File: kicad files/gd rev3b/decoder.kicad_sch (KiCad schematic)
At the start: 18 parts, among them U25 SN74LVC573ANS

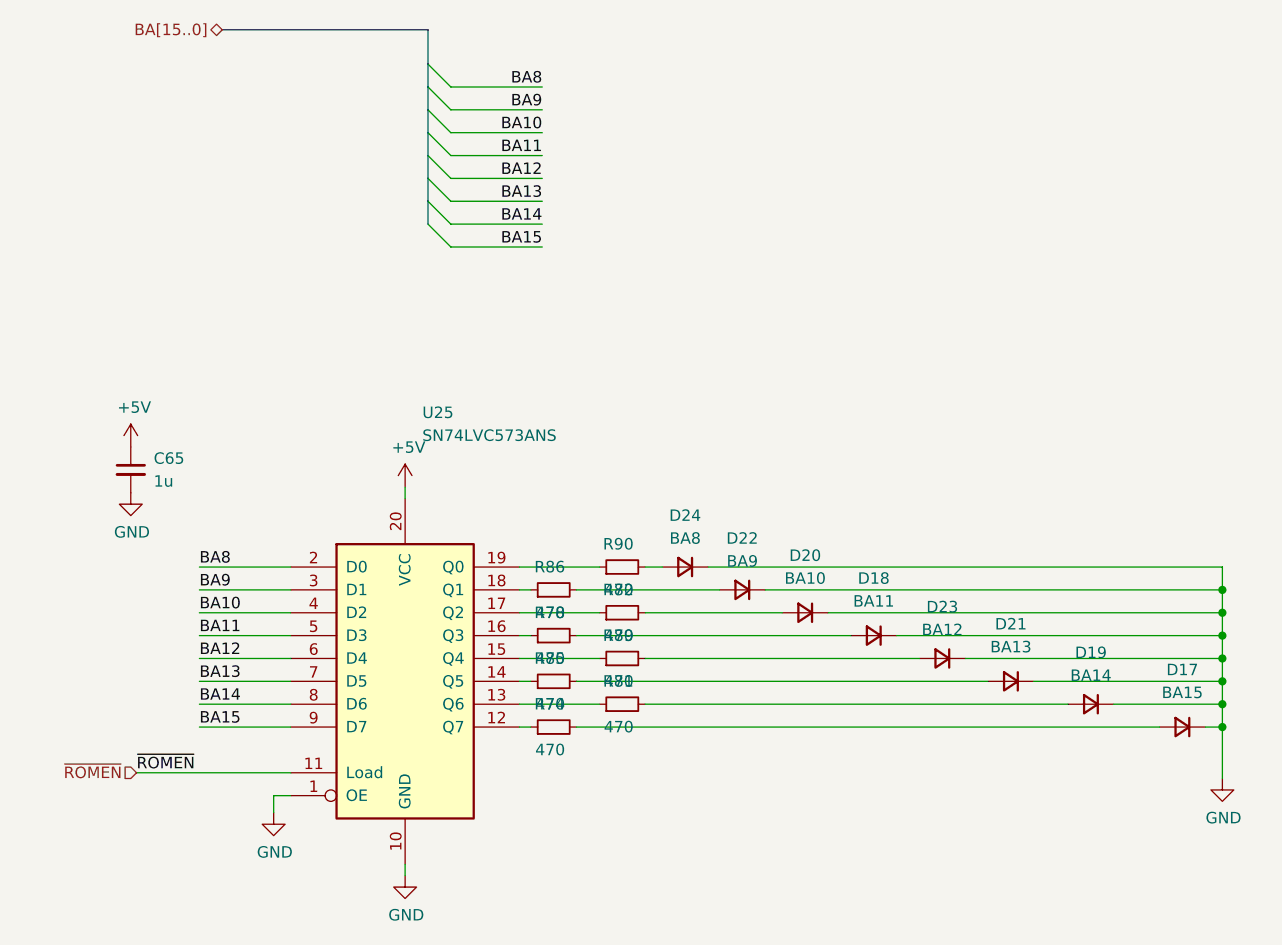
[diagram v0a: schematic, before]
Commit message: Schematic changes for #52, #50, #70, #51, #61, #69, #71
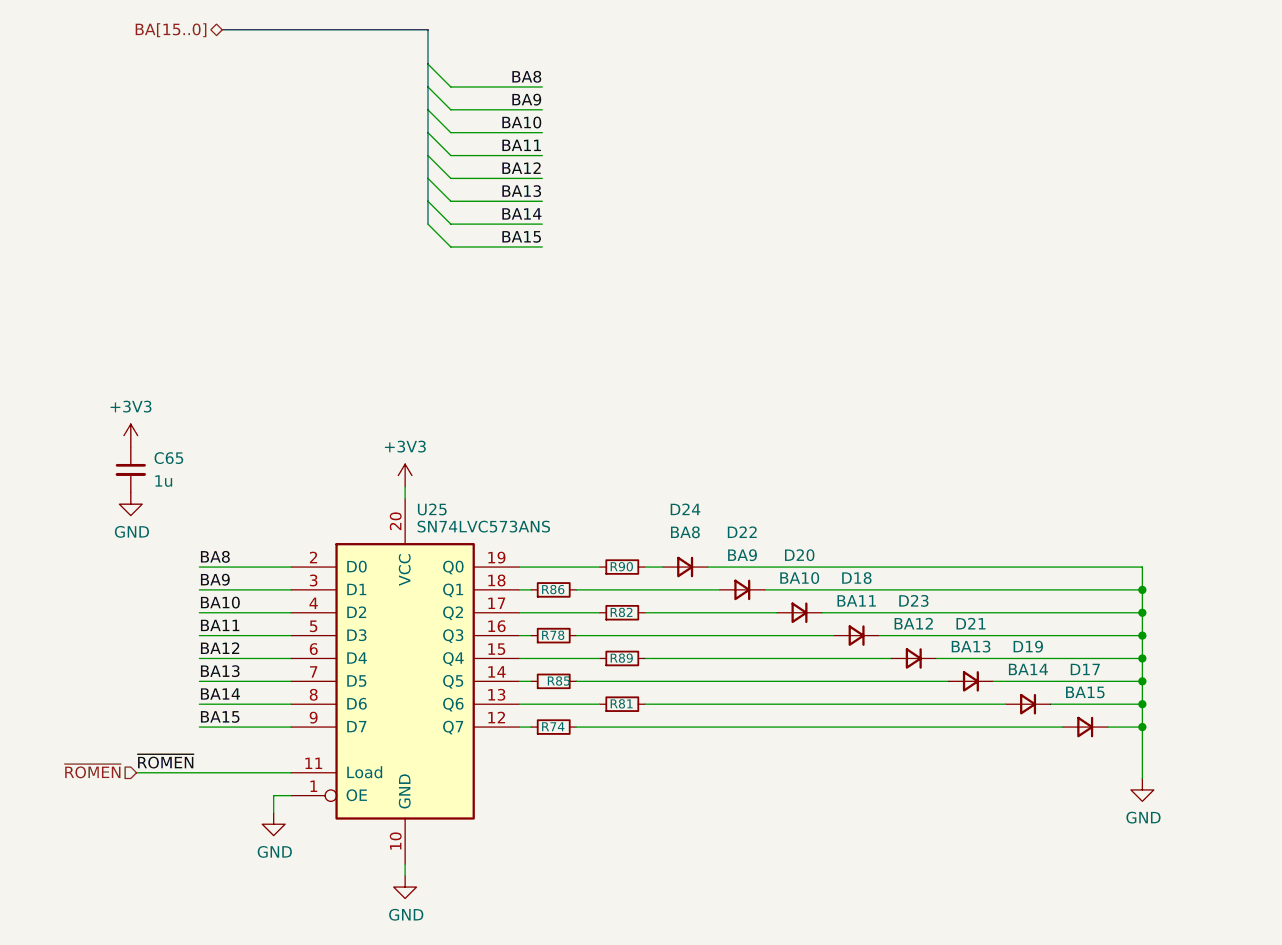
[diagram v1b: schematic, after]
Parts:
- R74, R78, R81, R82, R85, R86, R89, R90: value 470 -> 1k
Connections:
- net +5V renamed +3V3
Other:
- moved on the sheet: D17, D18, D19, D20, D21, D23

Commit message: added Linear for Decoder to fix #69
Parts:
- added C30: 1u, Capacitor_SMD:C_0805_2012Metric, symbol Mega IIe Rev3 Symbols:C
- added U15: MIC5504-3.3YM5, Package_TO_SOT_SMD:SOT-23-5, symbol Mega IIe Rev3 Symbols:MIC5504-3.3YM5
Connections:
- net GND: now also C30.2, U15.2 (GND)
- net +3V3 renamed +3V3_Decoder
- net +3V3_Decoder: now also U15.5 (VOUT)
- new net +5V: C30.1, U15.1 (VIN), U15.3 (EN)
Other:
- moved on the sheet: C65
